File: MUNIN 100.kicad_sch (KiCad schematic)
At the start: 78 parts, among them IC1 ACHS-7123, J1 TX_IN, J2 Conn_Coaxial, J3 Conn_01x03_Male, J4 3-647630-4, Q1 ISS55EP06LMXTSA1, Q2 MRF101AN, Q3 MRF101BN, U1 TL783CKTT, U2 LM358

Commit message: first pcb release
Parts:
- removed H1, H2, H3, H4: MH, MountingHole:MountingHole_3.2mm_M3, symbol Mechanical:MountingHole
- removed J4: 3-647630-4, Connector_PinHeader_2.54mm:PinHeader_1x04_P2.54mm_Horizontal, symbol Connector:Conn_01x04_Male
- removed U1: TL783CKTT, Package_TO_SOT_SMD:TO-263-3_TabPin2, symbol KjellKarlsen:TLV760-5V
- added H1, H2, H3, H4: MountingHole_Pad, MountingHole:MountingHole_3.2mm_M3_Pad_Via, symbol Mechanical:MountingHole_Pad
- added J4, J5: Conn_01x01_Pin, 7461057:7461057, symbol Connector:Conn_01x01_Pin
- added U3: TL783, Package_TO_SOT_SMD:TO-263-3_TabPin2, symbol TL783:TL783
- J1, J2: footprint Connector_Coaxial:SMA_Amphenol_132291_Vertical -> SMA_PINS:SMA_PINS
- J3: footprint Connector_PinHeader_2.54mm:PinHeader_1x03_P2.54mm_Horizontal -> Connector_Molex:Molex_KK-254_AE-6410-03A_1x03_P2.54mm_Vertical
- L2: value WuryhElek: 742792096 -> Wurth: 742792096
- L3: footprint LA2NI:FT_50_1 -> T50:T50_V_smd
- L5: footprint Inductor_SMD:L_1812_4532Metric -> Resistor_THT:R_Axial_DIN0918_L18.0mm_D9.0mm_P30.48mm_Horizontal
- TLT1: footprint LA2NI:TLT_94_3 -> TLT:TLT
- TLT2: footprint LA2NI:TLT_94_3 -> Amidon_Binocular:Dual_FB-61-4852
- U2: footprint Package_SO:Diodes_PSOP-8 -> Package_SO:SOIC-8_3.9x4.9mm_P1.27mm
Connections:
- net +5V: now also U3.2 (OUT)
- net GND: now also RV2.1, H1.1, H2.1, H3.1, H4.1, J5.1 (Pin_1); no longer RV2.3
- net at C9.1, Q1.2 (S): now also U3.3 (IN)
- net at C4.1, C7.1, L2.1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: now also RV2.3; no longer RV2.1
- net at R7.1, R8.2: now also U3.1 (ADJ)
- net at C14.2, C17.2: now also TLT2.1; no longer TLT2.4
- net at C21.1, C22.1, C23.1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: now also J4.1 (Pin_1)
- net at C15.2, C16.2: now also TLT2.4; no longer TLT2.1
- no-connect marks 0 -> 1

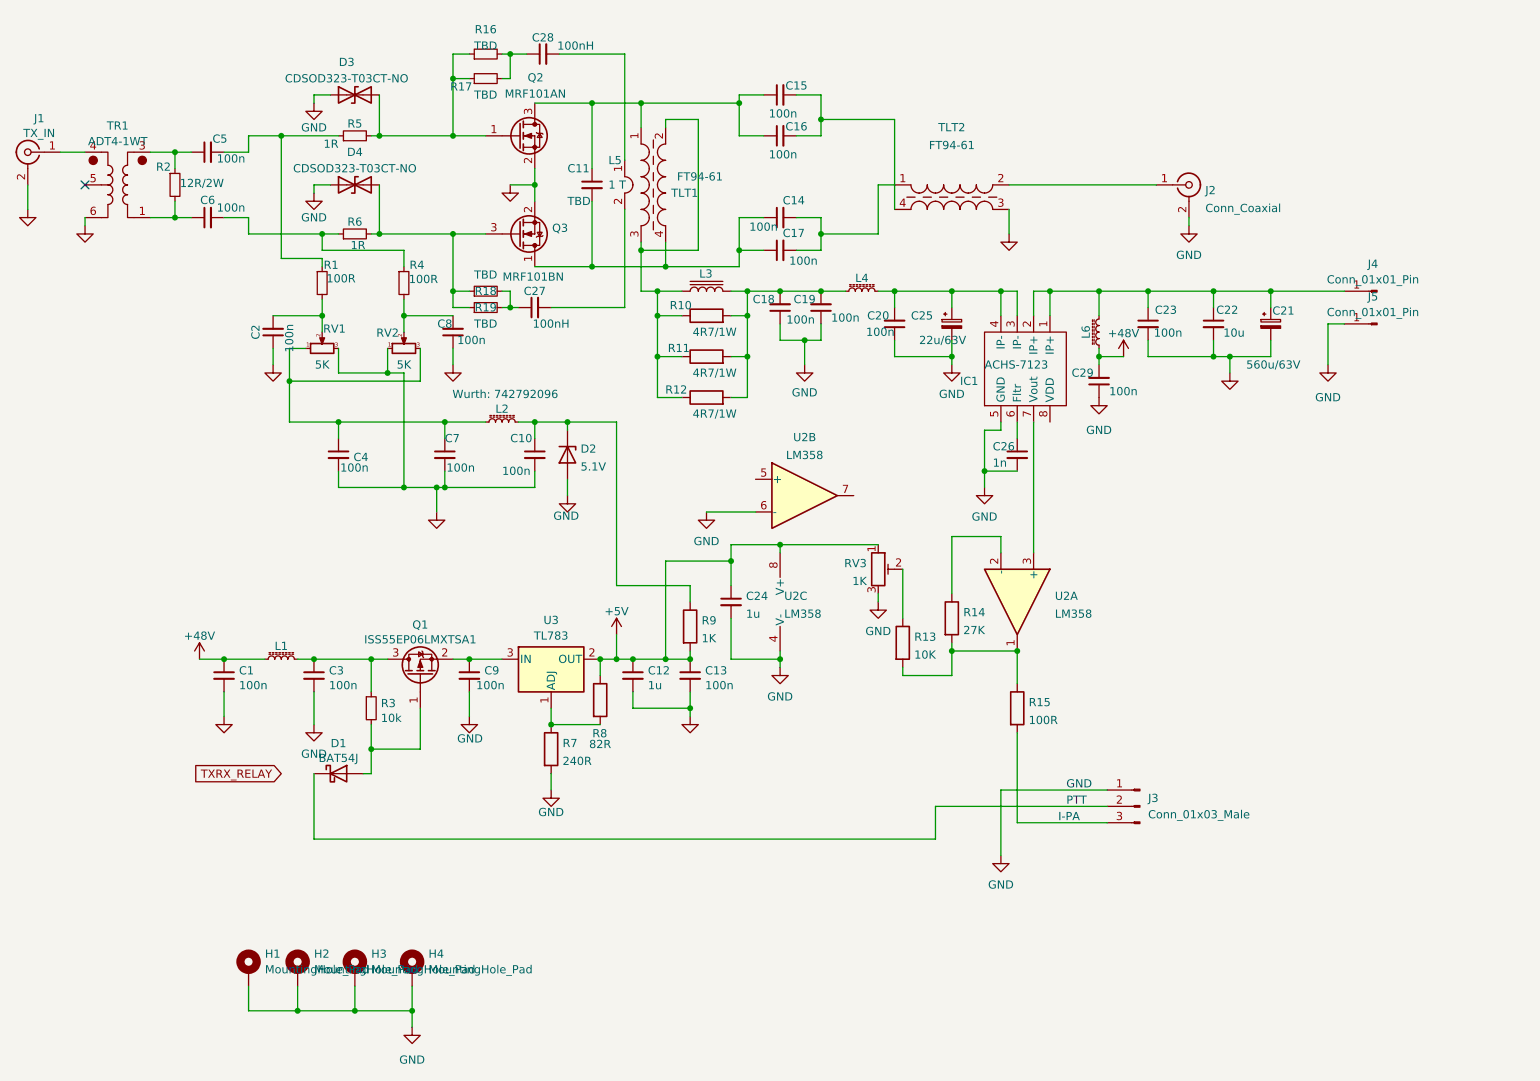
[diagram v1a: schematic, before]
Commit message: minor errors fixed, Gerber is out of date
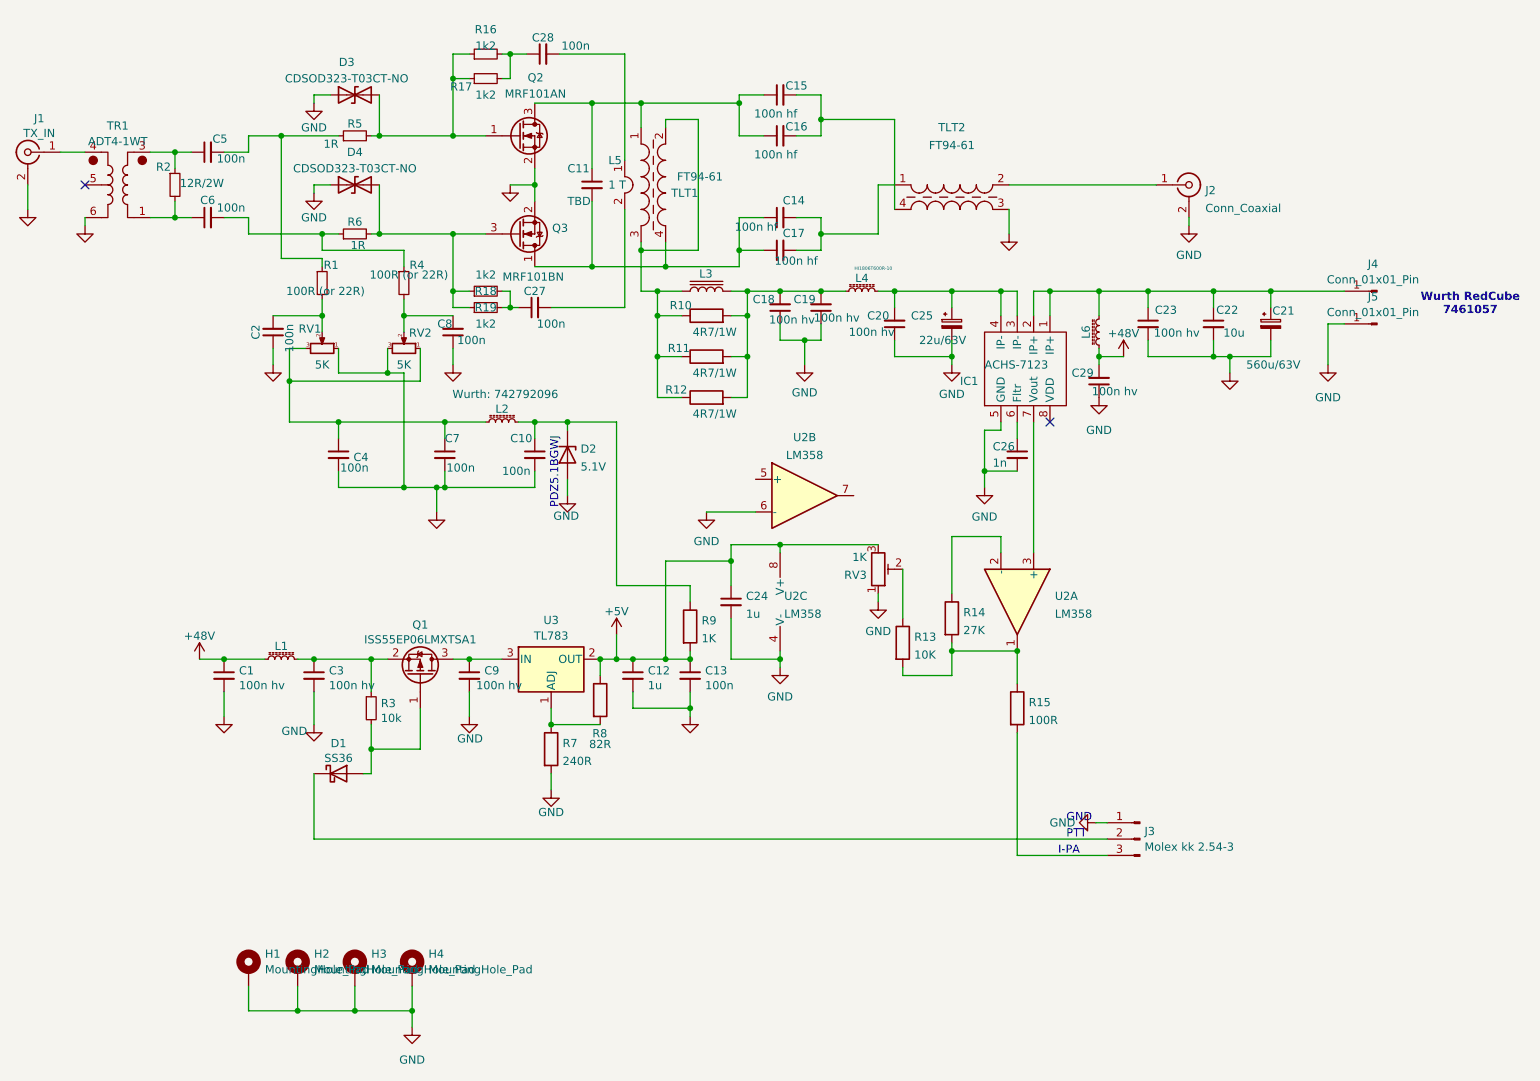
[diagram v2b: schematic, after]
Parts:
- C1: value 100n -> 100n hv; footprint Capacitor_SMD:C_0805_2012Metric -> Capacitor_SMD:C_0805_2012Metric_Pad1.18x1.45mm_HandSolder
- C14, C15, C16, C17: value 100n -> 100n hf
- C18, C19, C20, C23, C29, C3, C9: value 100n -> 100n hv
- C27, C28: value 100nH -> 100n
- D1: value BAT54J -> SS36; footprint Diode_SMD:D_MELF -> Diode_SMD:D_SOD-323_HandSoldering
- D2: footprint Diode_SMD:D_0603_1608Metric -> Diode_SMD:D_SOD-123F
- J3: value Conn_01x03_Male -> Molex kk 2.54-3
- R1, R4: value 100R -> 100R (or 22R)
- R16, R17, R18, R19: value TBD -> 1k2
- RV1, RV2, RV3: footprint Potentiometer_SMD:Potentiometer_Bourns_3214G_Horizontal -> Potentiometer_SMD:Potentiometer_Bourns_3214X_Vertical
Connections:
- net +5V: now also RV3.3; no longer RV3.1
- net GND: now also RV1.1, RV2.3, RV3.1; no longer RV1.3, RV2.1, RV3.3
- net at C9.1, U3.3 (IN): now also Q1.3 (D); no longer Q1.2 (S)
- net at C4.1, C7.1, L2.1: now also RV1.3, RV2.1; no longer RV1.1, RV2.3
- net at C3.1, L1.2, R3.1: now also Q1.2 (S); no longer Q1.3 (D)
- no-connect marks 1 -> 2
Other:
- note added: "PDZ5.1BGWJ"
- note added: "Wurth RedCube 7461057"
- moved on the sheet: J3, Q1, RV1, RV2

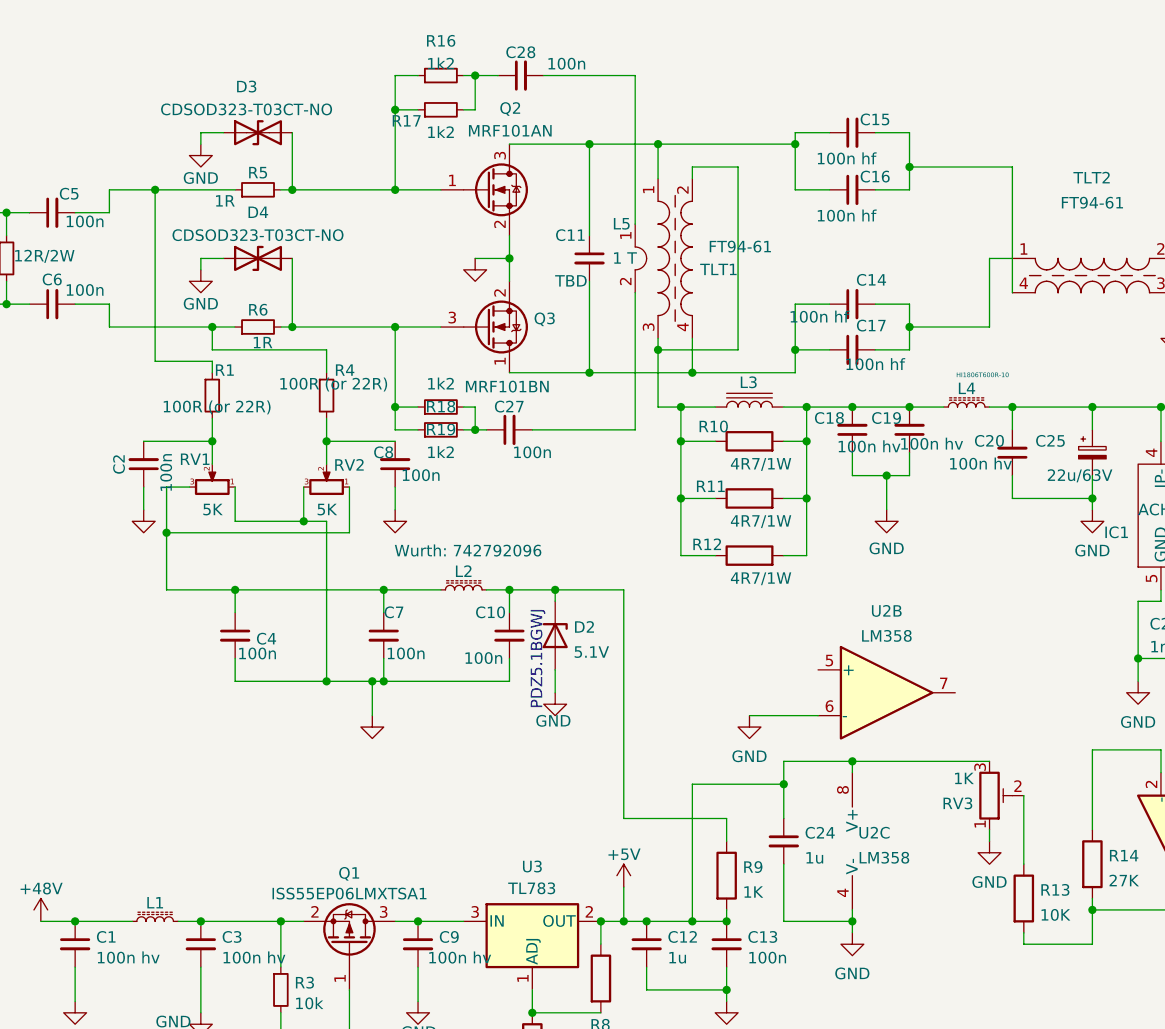
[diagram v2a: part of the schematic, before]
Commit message: new 48V trace
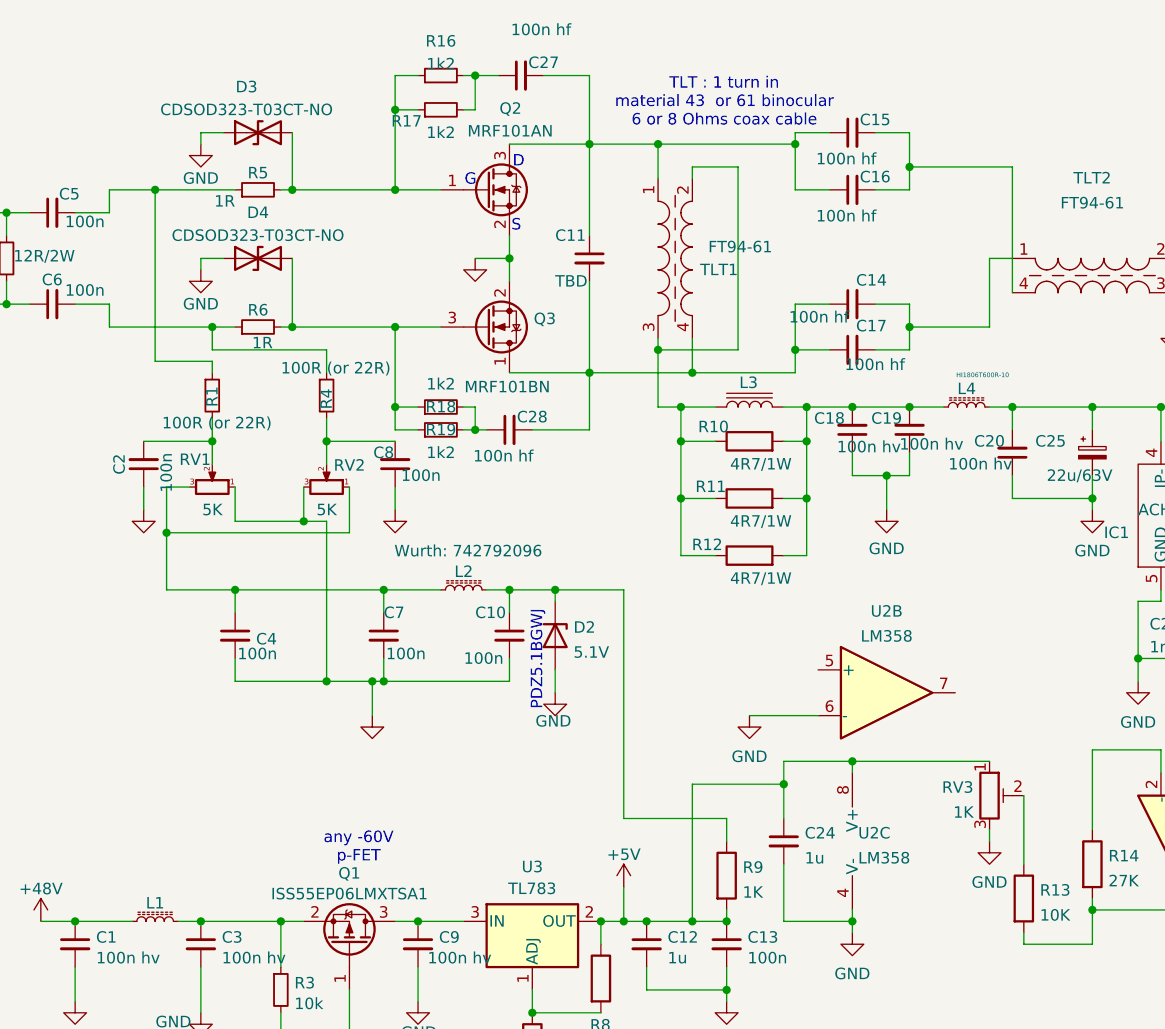
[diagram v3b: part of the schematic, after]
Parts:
- removed C27, C28: 100n, Capacitor_SMD:C_0805_2012Metric, symbol Device:C_Small
- removed L5: 1 T, Resistor_THT:R_Axial_DIN0918_L18.0mm_D9.0mm_P30.48mm_Horizontal, symbol LA2NI:FB_Link
- added C27, C28: 100n hf, Capacitor_SMD:C_1210_3225Metric_Pad1.33x2.70mm_HandSolder, symbol KjellKarlsen:C_Small
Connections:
- net +5V: now also RV3.1; no longer RV3.3
- net GND: now also RV3.3; no longer RV3.1
- net at R18.2, R19.2: now also C28.1
- net at R16.2, R17.2: now also C27.1
- net at C11.2, C14.1, C17.1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: now also C28.2
- net at C11.1, C15.1, C16.1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: now also C27.2
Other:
- note added: "D"
- note added: "G"
- note added: "S"
- note added: "TLT : 1 turn in material 43 or 61 binocular 6 or 8 Ohms coax cable"
- note added: "any -60V p-FET"
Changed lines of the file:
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@@
 	(wire
 		(pts
+			(xy 106.68 66.04) (xy 113.03 66.04)
+		)
+		(stroke
+			(width 0)
+			(type default)
+		)
+	)
+	(wire
+		(pts
 			(xy 91.44 26.67) (xy 91.44 30.48)
 		)
@@
 	(wire
 		(pts
-			(xy 107.95 26.67) (xy 118.11 26.67)
-		)
-		(stroke
-			(width 0)
-			(type default)
-		)
-	)
-	(wire
-		(pts
 			(xy 124.46 120.65) (xy 128.27 120.65)
 		)
@@
 	(wire
 		(pts
+			(xy 113.03 26.67) (xy 113.03 34.29)
+		)
+		(stroke
+			(width 0)
+			(type default)
+		)
+	)
+	(wire
+		(pts
 			(xy 67.31 175.26) (xy 76.2 175.26)
 		)
@@
 	(wire
 		(pts
-			(xy 118.11 50.8) (xy 118.11 66.04)
-		)
-		(stroke
-			(width 0)
-			(type default)
-		)
-	)
-	(wire
-		(pts
 			(xy 104.14 59.69) (xy 113.03 59.69)
 		)
@@
 	(wire
 		(pts
-			(xy 118.11 26.67) (xy 118.11 43.18)
-		)
-		(stroke
-			(width 0)
-			(type default)
-		)
-	)
-	(wire
-		(pts
 			(xy 191.77 63.5) (xy 191.77 67.31)
 		)
@@
 	(wire
 		(pts
-			(xy 106.68 66.04) (xy 118.11 66.04)
-		)
-		(stroke
-			(width 0)
-			(type default)
-		)
-	)
-	(wire
-		(pts
 			(xy 128.27 119.38) (xy 128.27 120.65)
 		)
@@
 	(wire
 		(pts
+			(xy 107.95 26.67) (xy 113.03 26.67)
+		)
+		(stroke
+			(width 0)
+			(type default)
+		)
+	)
+	(wire
+		(pts
 			(xy 177.8 50.8) (xy 177.8 54.61)
 		)
@@
 	(wire
 		(pts
+			(xy 113.03 66.04) (xy 113.03 59.69)
+		)
+		(stroke
+			(width 0)
+			(type default)
+		)
+	)
+	(wire
+		(pts
 			(xy 160.02 73.66) (xy 168.91 73.66)
 		)
@@
 		)
 	)
+	(text "S\n"
+		(exclude_from_sim no)
+		(at 104.902 43.434 0)
+		(effects
+			(font
+				(size 1.27 1.27)
+			)
+		)
+	)
 	(text "PDZ5.1BGWJ"
 		(exclude_from_sim no)
@@
 		)
 	)
+	(text "D"
+		(exclude_from_sim no)
+		(at 105.156 36.322 0)
+		(effects
+			(font
+				(size 1.27 1.27)
+			)
+		)
+	)
 	(text "GND"
 		(exclude_from_sim no)
@@
 		)
 	)
+	(text "TLT : 1 turn in \nmaterial 43  or 61 binocular \n6 or 8 Ohms coax cable\n"
+		(exclude_from_sim no)
+		(at 128.016 29.718 0)
+		(effects
+			(font
+				(size 1.27 1.27)
+			)
+		)
+	)
 	(text "PTT"
 		(exclude_from_sim no)
@@
 		)
 	)
+	(text "any -60V\np-FET "
+		(exclude_from_sim no)
+		(at 87.376 112.522 0)
+		(effects
+			(font
+				(size 1.27 1.27)
+			)
+		)
+	)
+	(text "G\n"
+		(exclude_from_sim no)
+		(at 99.822 38.354 0)
+		(effects
+			(font
+				(size 1.27 1.27)
+			)
+		)
+	)
 	(symbol
 		(lib_id "KjellKarlsen:R_Small")
@@
 		(lib_id "Device:R_POT_TRIM")
 		(at 157.48 106.68 0)
-		(mirror x)
 		(unit 1)
 		(exclude_from_sim no)
@@
 		(dnp no)
 		(property "Reference" "RV3"
-			(at 155.7021 107.5885 0)
+			(at 155.7021 105.7715 0)
 			(effects
 				(font
@@
 		)
 		(property "Value" "1K"
-			(at 155.7021 104.8134 0)
+			(at 155.7021 108.5466 0)
 			(effects
 				(font
@@
 	)
 	(symbol
-		(lib_id "Device:C_Small")
+		(lib_id "KjellKarlsen:C_Small")
 		(at 104.14 66.04 90)
 		(unit 1)
@@
 		(on_board yes)
 		(dnp no)
-		(property "Reference" "C27"
-			(at 104.14 63.5 90)
+		(property "Reference" "C28"
+			(at 106.68 64.6135 90)
 			(effects
 				(font
@@
 			)
 		)
-		(property "Value" "100n"
-			(at 106.68 68.58 90)
+		(property "Value" "100n hf"
+			(at 106.807 68.961 90)
 			(effects
 				(font
 					(size 1.27 1.27)
 				)
+				(justify left)
 			)
 		)
-		(property "Footprint" "Capacitor_SMD:C_0805_2012Metric"
+		(property "Footprint" "Capacitor_SMD:C_1210_3225Metric_Pad1.33x2.70mm_HandSolder"
 			(at 104.14 66.04 0)
 			(effects
@@
 			(project "MUNIN 100"
 				(path "/23397694-a57f-4fcf-95b5-f9e2ccb3d33d"
-					(reference "C27")
+					(reference "C28")
 					(unit 1)
 				)
@@
 		(dnp no)
 		(property "Reference" "R4"
-			(at 84.6837 59.4435 0)
+			(at 83.82 63.754 90)
 			(effects
 				(font
@@
 		)
 		(property "Value" "100R (or 22R)"
-			(at 78.486 60.96 0)
+			(at 78.74 59.182 0)
 			(effects
 				(font
@@
 		(dnp no)
 		(property "Reference" "R1"
-			(at 71.3487 59.4435 0)
+			(at 71.12 63.5 90)
 			(effects
 				(font
@@
 		)
 		(property "Value" "100R (or 22R)"
-			(at 65.532 63.5 0)
+			(at 65.532 65.278 0)
 			(effects
 				(font
@@
 	)
 	(symbol
+		(lib_id "KjellKarlsen:C_Small")
+		(at 105.41 26.67 90)
+		(unit 1)
+		(exclude_from_sim no)
+		(in_bom yes)
+		(on_board yes)
+		(dnp no)
+		(property "Reference" "C27"
+			(at 107.95 25.2435 90)
+			(effects
+				(font
+					(size 1.27 1.27)
+				)
+			)
+		)
+		(property "Value" "100n hf"
+			(at 110.998 21.59 90)
+			(effects
+				(font
+					(size 1.27 1.27)
+				)
+				(justify left)
+			)
+		)
+		(property "Footprint" "Capacitor_SMD:C_1210_3225Metric_Pad1.33x2.70mm_HandSolder"
+			(at 105.41 26.67 0)
+			(effects
+				(font
+					(size 1.27 1.27)
+				)
+				(hide yes)
+			)
+		)
+		(property "Datasheet" "~"
+			(at 105.41 26.67 0)
+			(effects
+				(font
+					(size 1.27 1.27)
+				)
+				(hide yes)
+			)
+		)
+		(property "Description" ""
+			(at 105.41 26.67 0)
+			(effects
+				(font
+					(size 1.27 1.27)
+				)
+				(hide yes)
+			)
+		)
+		(pin "1"
+		)
+		(pin "2"
+		)
+		(instances
+			(project "MUNIN 100"
+				(path "/23397694-a57f-4fcf-95b5-f9e2ccb3d33d"
+					(reference "C27")
+					(unit 1)
+				)
+			)
+		)
+	)
+	(symbol
 		(lib_id "Amplifier_Operational:LMV358")
 		(at 146.05 95.25 0)
@@
 	)
 	(symbol
-		(lib_id "LA2NI:FB_Link")
-		(at 118.11 45.72 0)
-		(unit 1)
-		(exclude_from_sim no)
-		(in_bom yes)
-		(on_board yes)
-		(dnp no)
-		(property "Reference" "L5"
-			(at 115.57 43.18 0)
-			(effects
-				(font
-					(size 1.27 1.27)
-				)
-				(justify left)
-			)
-		)
-		(property "Value" "1 T"
-			(at 115.57 46.99 0)
-			(effects
-				(font
-					(size 1.27 1.27)
-				)
-				(justify left)
-			)
-		)
-		(property "Footprint" "Resistor_THT:R_Axial_DIN0918_L18.0mm_D9.0mm_P30.48mm_Horizontal"
-			(at 118.11 45.72 0)
-			(effects
-				(font
-					(size 1.27 1.27)
-				)
-				(hide yes)
-			)
-		)
-		(property "Datasheet" ""
-			(at 118.11 45.72 0)
-			(effects
-				(font
-					(size 1.27 1.27)
-				)
-				(hide yes)
-			)
-		)
-		(property "Description" ""
-			(at 118.11 45.72 0)
-			(effects
-				(font
-					(size 1.27 1.27)
-				)
-				(hide yes)
-			)
-		)
-		(pin "1"
-		)
-		(pin "2"
-		)
-		(instances
-			(project "MUNIN 100"
-				(path "/23397694-a57f-4fcf-95b5-f9e2ccb3d33d"
-					(reference "L5")
-					(unit 1)
-				)
-			)
-		)
-	)
-	(symbol
 		(lib_id "KjellKarlsen:C_Small")
 		(at 91.44 69.85 180)
@@
 					(unit 1)
 				)
-			)
-		)
-	)
-	(symbol
-		(lib_id "Device:C_Small")
-		(at 105.41 26.67 90)
-		(unit 1)
-		(exclude_from_sim no)
-		(in_bom yes)
-		(on_board yes)
-		(dnp no)
-		(property "Reference" "C28"
-			(at 105.41 24.13 90)
-			(effects
-				(font
-					(size 1.27 1.27)
-				)
-			)
-		)
-		(property "Value" "100n"
-			(at 110.49 25.4 90)
-			(effects
-				(font
-					(size 1.27 1.27)
-				)
-			)
-		)
-		(property "Footprint" "Capacitor_SMD:C_0805_2012Metric"
-			(at 105.41 26.67 0)
-			(effects
-				(font
-					(size 1.27 1.27)
-				)
-				(hide yes)
-			)
-		)
-		(property "Datasheet" "~"
-			(at 105.41 26.67 0)
-			(effects
-				(font
-					(size 1.27 1.27)
-				)
-				(hide yes)
-			)
-		)
-		(property "Description" ""
-			(at 105.41 26.67 0)
-			(effects
-				(font
-					(size 1.27 1.27)
-				)
-				(hide yes)
-			)
-		)
-		(pin "1"
-		)
-		(pin "2"
-		)
-		(instances
-			(project "MUNIN 100"
-				(path "/23397694-a57f-4fcf-95b5-f9e2ccb3d33d"
-					(reference "C28")
-					(unit 1)
-				)
